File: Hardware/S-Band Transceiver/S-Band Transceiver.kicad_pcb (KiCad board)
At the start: 4 copper layers, 127 x 101.6 mm, 224 parts, among them J1 SMA, J2 SMA, J3 AVR-UPDI-6, J4 USB_C_Receptacle_USB2.0_16P, J5 SMA, J6 SMA, J7 SMA, J8 SMA, SW1 SW_Push, U1 ADF4351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

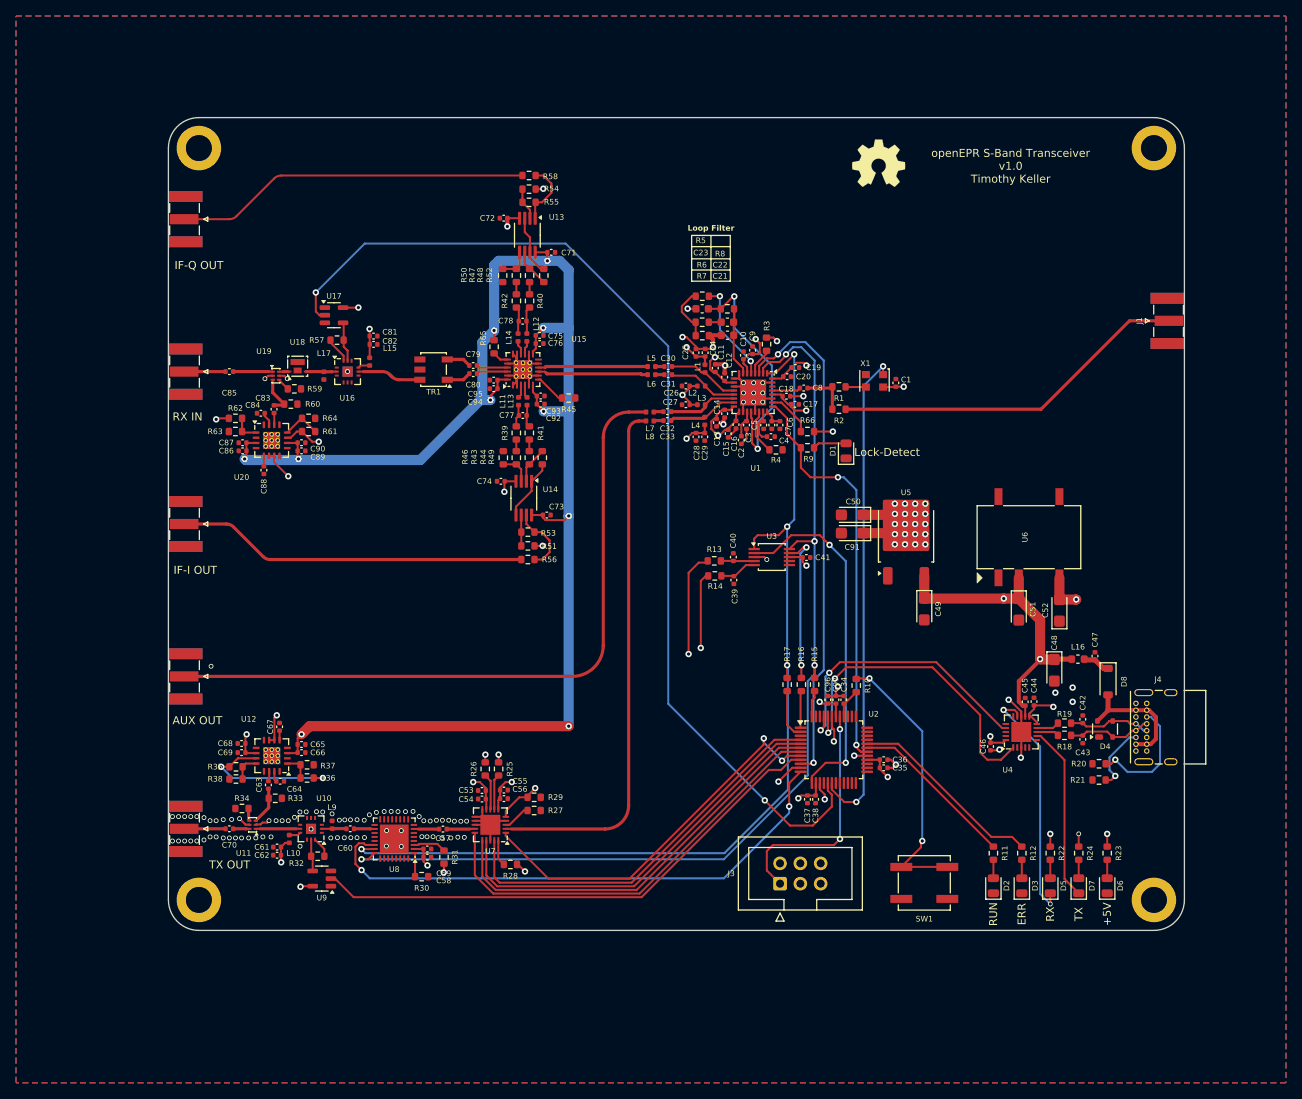
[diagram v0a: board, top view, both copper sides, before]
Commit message: Removing solder mask from coplanar waveguide traces
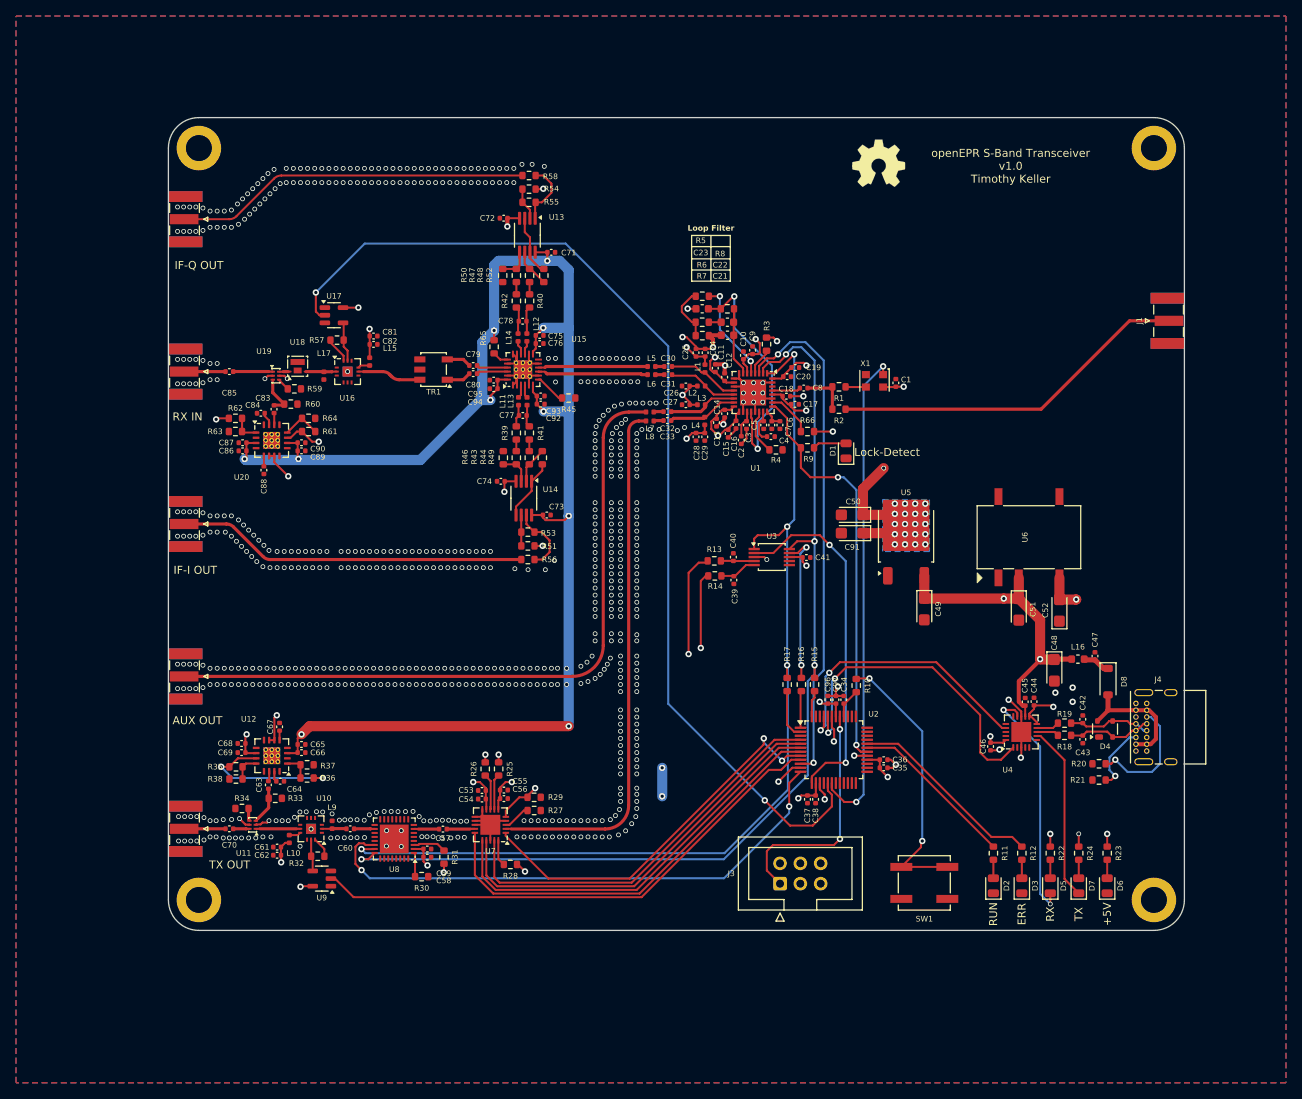
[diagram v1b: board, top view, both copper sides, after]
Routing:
- net +3.3VA: track 93.2 -> 103.6 mm, vias 42 -> 45
- net RX_VRMS: track 73.9 -> 77.9 mm
- net GND: vias 111 -> 660
- added copper zone on B.Cu, net +3.3VA

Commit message: Updates to Board
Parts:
- moved L17 0.18 mm to (82.8, 57.7)
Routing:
- net GND: vias 660 -> 716

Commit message: Updates to schematic
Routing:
- net GND: track 86.8 -> 90.9 mm, vias 716 -> 769

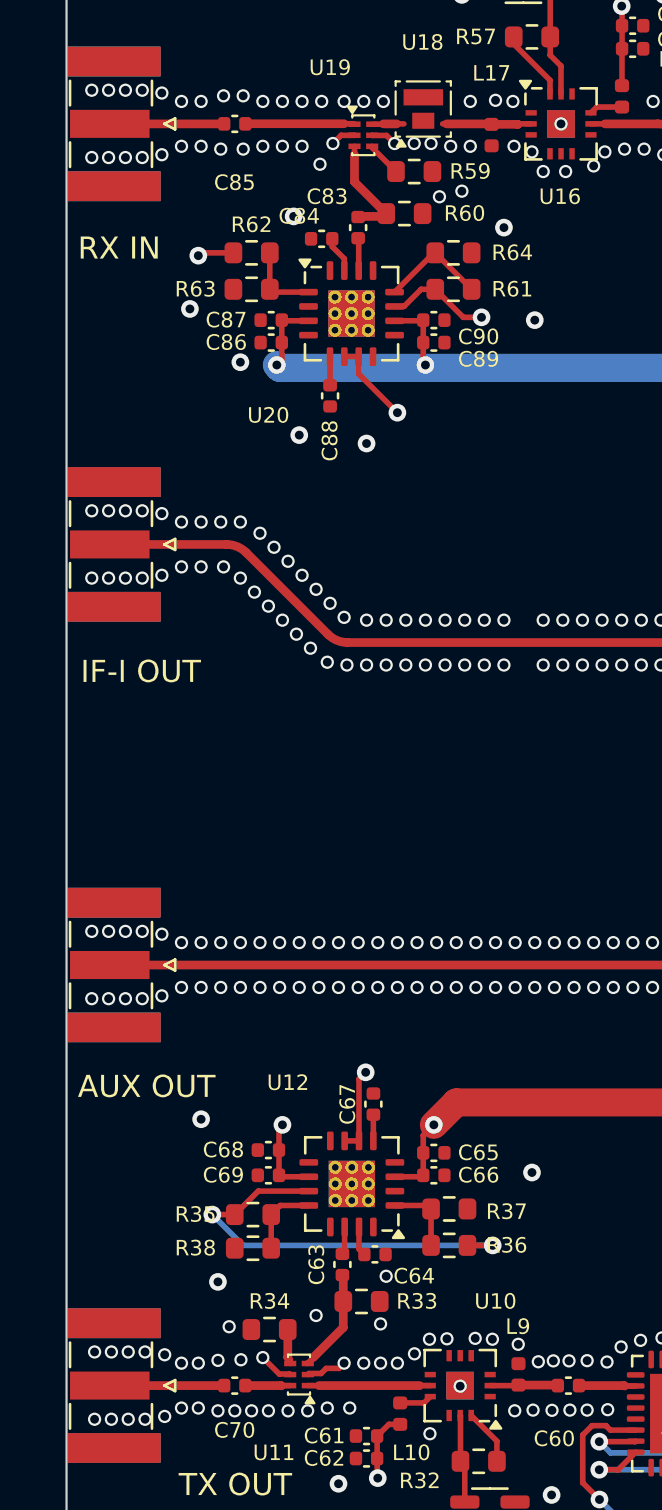
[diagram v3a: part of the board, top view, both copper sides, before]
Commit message: Updating notes in schematic
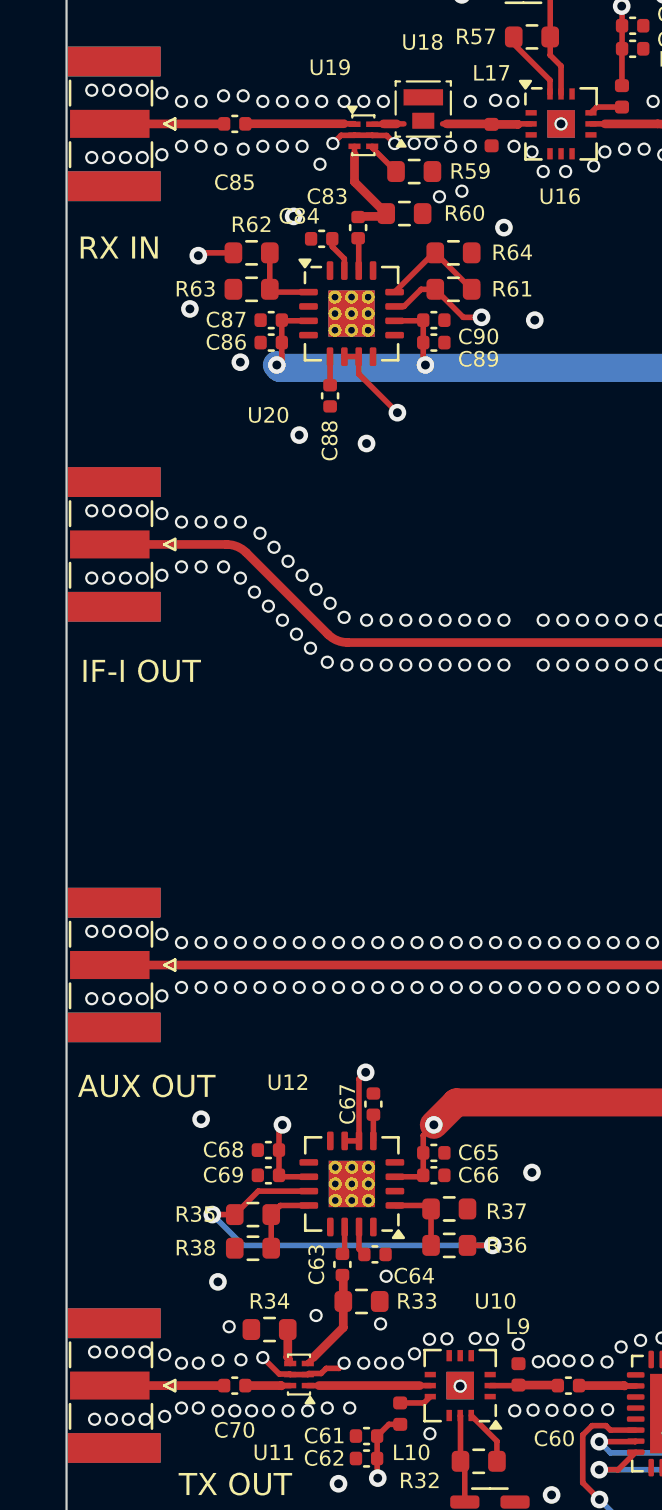
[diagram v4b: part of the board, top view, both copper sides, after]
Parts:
- C57, C60, C63, C64, C70, C79, C80, C83, C84, C85: value 10nF -> 10000pF
- J1, J2, J5, J6, J7, J8: value SMA -> SMA-J-P-H-ST-EM1
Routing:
- net GND: track 90.9 -> 92.5 mm

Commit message: Adding gerbers for v1.0
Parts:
- D4: value SP0503BAHT -> SP0503BAHTG
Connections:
- U2 pad 3: ~{CS} -> unconnected-(U2-PA7-Pad3)
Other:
- board text added: "REF"
